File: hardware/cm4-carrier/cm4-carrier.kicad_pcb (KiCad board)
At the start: 2 copper layers, 121 x 76 mm, 0 parts

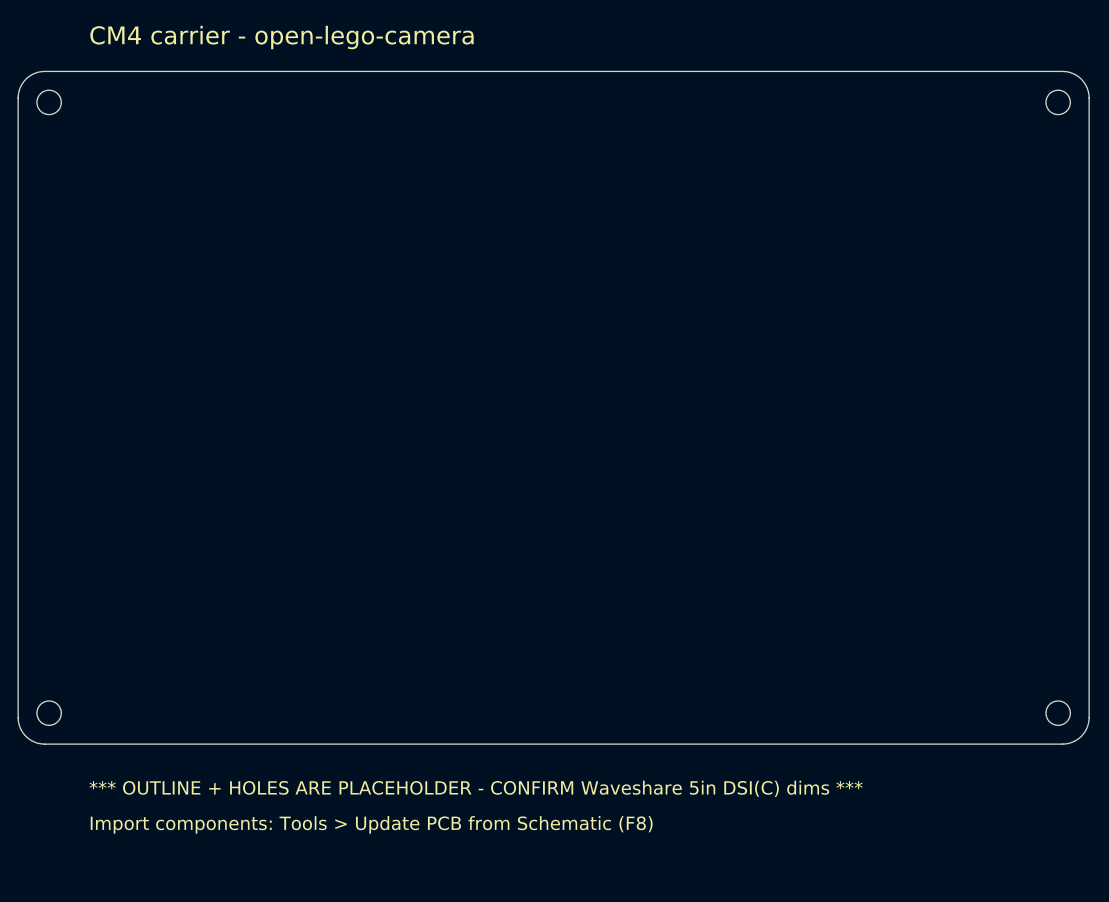
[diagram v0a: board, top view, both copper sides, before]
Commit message: Set PCB outline and mounting holes from Waveshare 5in DSI (C) STEP
Replace the placeholder board dimensions with values extracted from the
supplied Waveshare 5inch DSI LCD (C) STEP model:

- Outline 120.70 x 77.20 mm (display module X/Y extent, 3 mm rounded corners).
- Four M2.5 mounting holes (Ø2.75 mm) on a 113.0 x 68.0 mm rectangle, matching
  the display's STUDS-M2_5XH4 back studs at (+/-56.5, -35.9/+32.1) so the
  carrier bolts directly onto the display.

Silkscreen notes and README updated to the confirmed dimensions.

Co-Authored-By: Claude Opus 4.8 <noreply@anthropic.com>
Claude-Session: https://claude.ai/code/session_015B7X7FE461jFSRaiTFdnFt
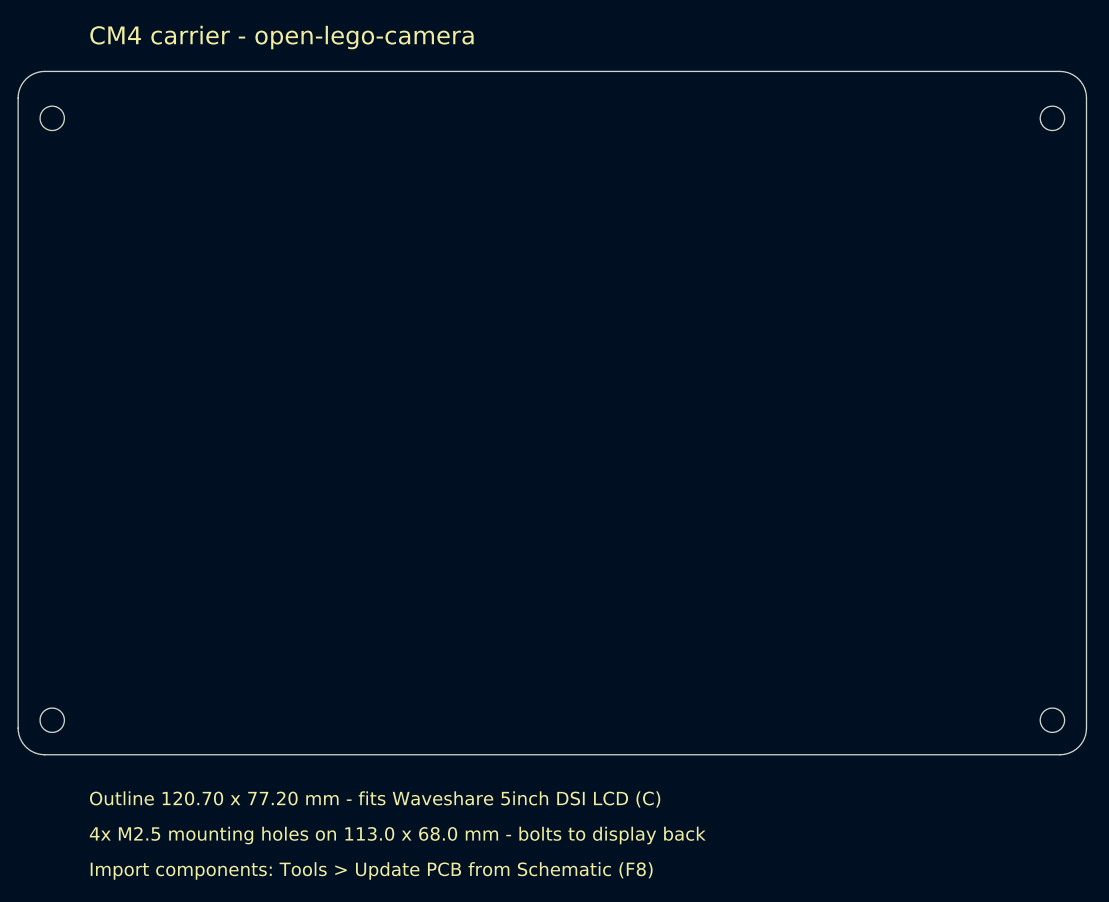
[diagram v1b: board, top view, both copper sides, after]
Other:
- board size 121 x 76 mm -> 120.7 x 77.2 mm
- board text added: "4x M2.5 mounting holes on 113.0 x 68.0 mm - bolts to display back"
- board text added: "Outline 120.70 x 77.20 mm - fits Waveshare 5inch DSI LCD (C)"
- board text removed: "*** OUTLINE + HOLES ARE PLACEHOLDER - CONFIRM Waveshare 5in DSI(C) dims ***"
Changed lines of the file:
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@@
 	)
 	(net 0 "")
-	(gr_line (start 63.000 40.000) (end 178.000 40.000)
+	(gr_line (start 63.000 40.000) (end 177.700 40.000)
 		(stroke (width 0.1) (type solid)) (layer "Edge.Cuts"))
-	(gr_line (start 181.000 43.000) (end 181.000 113.000)
+	(gr_line (start 180.700 43.000) (end 180.700 114.200)
 		(stroke (width 0.1) (type solid)) (layer "Edge.Cuts"))
-	(gr_line (start 178.000 116.000) (end 63.000 116.000)
+	(gr_line (start 177.700 117.200) (end 63.000 117.200)
 		(stroke (width 0.1) (type solid)) (layer "Edge.Cuts"))
-	(gr_line (start 60.000 113.000) (end 60.000 43.000)
+	(gr_line (start 60.000 114.200) (end 60.000 43.000)
 		(stroke (width 0.1) (type solid)) (layer "Edge.Cuts"))
 	(gr_arc (start 60.000 43.000) (mid 60.879 40.879) (end 63.000 40.000)
 		(stroke (width 0.1) (type solid)) (layer "Edge.Cuts"))
-	(gr_arc (start 178.000 40.000) (mid 180.121 40.879) (end 181.000 43.000)
+	(gr_arc (start 177.700 40.000) (mid 179.821 40.879) (end 180.700 43.000)
 		(stroke (width 0.1) (type solid)) (layer "Edge.Cuts"))
-	(gr_arc (start 181.000 113.000) (mid 180.121 115.121) (end 178.000 116.000)
+	(gr_arc (start 180.700 114.200) (mid 179.821 116.321) (end 177.700 117.200)
 		(stroke (width 0.1) (type solid)) (layer "Edge.Cuts"))
-	(gr_arc (start 63.000 116.000) (mid 60.879 115.121) (end 60.000 113.000)
+	(gr_arc (start 63.000 117.200) (mid 60.879 116.321) (end 60.000 114.200)
 		(stroke (width 0.1) (type solid)) (layer "Edge.Cuts"))
-	(gr_circle (center 63.500 43.500) (end 64.875 43.500)
+	(gr_circle (center 63.850 45.300) (end 65.225 45.300)
 		(stroke (width 0.1) (type solid)) (fill none) (layer "Edge.Cuts"))
-	(gr_circle (center 177.500 43.500) (end 178.875 43.500)
+	(gr_circle (center 176.850 45.300) (end 178.225 45.300)
 		(stroke (width 0.1) (type solid)) (fill none) (layer "Edge.Cuts"))
-	(gr_circle (center 63.500 112.500) (end 64.875 112.500)
+	(gr_circle (center 63.850 113.300) (end 65.225 113.300)
 		(stroke (width 0.1) (type solid)) (fill none) (layer "Edge.Cuts"))
-	(gr_circle (center 177.500 112.500) (end 178.875 112.500)
+	(gr_circle (center 176.850 113.300) (end 178.225 113.300)
 		(stroke (width 0.1) (type solid)) (fill none) (layer "Edge.Cuts"))
 	(gr_text "CM4 carrier - open-lego-camera" (at 68.000 36.000)
 		(layer "F.SilkS")
 		(effects (font (size 2.0 2.0) (thickness 0.30)) (justify left)))
-	(gr_text "*** OUTLINE + HOLES ARE PLACEHOLDER - CONFIRM Waveshare 5in DSI(C) dims ***" (at 68.000 121.000)
+	(gr_text "Outline 120.70 x 77.20 mm - fits Waveshare 5inch DSI LCD (C)" (at 68.000 122.200)
 		(layer "F.SilkS")
 		(effects (font (size 1.5 1.5) (thickness 0.22)) (justify left)))
-	(gr_text "Import components: Tools > Update PCB from Schematic (F8)" (at 68.000 125.000)
+	(gr_text "4x M2.5 mounting holes on 113.0 x 68.0 mm - bolts to display back" (at 68.000 126.200)
 		(layer "F.SilkS")
 		(effects (font (size 1.5 1.5) (thickness 0.22)) (justify left)))
+	(gr_text "Import components: Tools > Update PCB from Schematic (F8)" (at 68.000 130.200)
+		(layer "F.SilkS")
+		(effects (font (size 1.5 1.5) (thickness 0.22)) (justify left)))

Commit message: PCB: MountingHole footprints + FPC connector keepout
- Replace the four Edge.Cuts hole cutouts with proper KiCad MountingHole
  footprints (H1-H4, MountingHole_2.7mm_M2.5, unplated np_thru_hole pads) at
  the display's M2.5 stud positions, so they are BOM/DRC-aware.
- Add a keepout rule area ("Display FPC connector clearance") over the display's
  back-side DSI FFC connector so no copper/components sit where it protrudes
  into the standoff gap, with a dashed Cmts.User outline and silkscreen note.

The exact FFC connector could not be labelled from the STEP assembly graph, so
the keepout is a single parameterised rectangle placed at the best-estimate
position (board-local ~(10,42) mm); README lists the other candidate connector
centres from the STEP so it can be moved. Kept as a keepout (not a board
cutout) since the studs give ~8 mm clearance.

Co-Authored-By: Claude Opus 4.8 <noreply@anthropic.com>
Claude-Session: https://claude.ai/code/session_015B7X7FE461jFSRaiTFdnFt
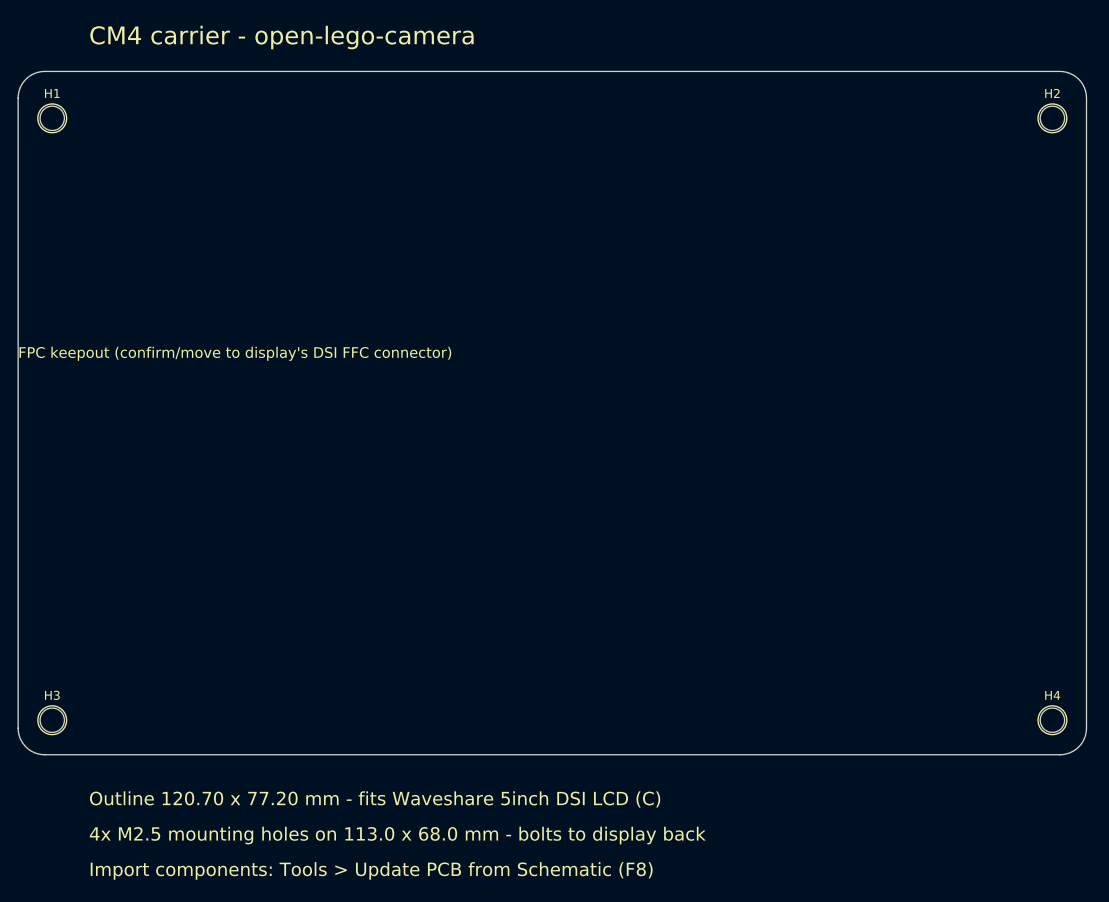
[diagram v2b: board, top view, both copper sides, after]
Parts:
- added H1: MountingHole_M2.5, MountingHole:MountingHole_2.7mm_M2.5, F.Cu at (63.9, 45.3)
- added H2: MountingHole_M2.5, MountingHole:MountingHole_2.7mm_M2.5, F.Cu at (176.8, 45.3)
- added H3: MountingHole_M2.5, MountingHole:MountingHole_2.7mm_M2.5, F.Cu at (63.9, 113.3)
- added H4: MountingHole_M2.5, MountingHole:MountingHole_2.7mm_M2.5, F.Cu at (176.8, 113.3)
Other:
- outline, holes or cut-outs redrawn
- board text added: "FPC keepout (confirm/move to display's DSI FFC connector)"
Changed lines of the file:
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@@
 	(gr_arc (start 63.000 117.200) (mid 60.879 116.321) (end 60.000 114.200)
 		(stroke (width 0.1) (type solid)) (layer "Edge.Cuts"))
-	(gr_circle (center 63.850 45.300) (end 65.225 45.300)
-		(stroke (width 0.1) (type solid)) (fill none) (layer "Edge.Cuts"))
-	(gr_circle (center 176.850 45.300) (end 178.225 45.300)
-		(stroke (width 0.1) (type solid)) (fill none) (layer "Edge.Cuts"))
-	(gr_circle (center 63.850 113.300) (end 65.225 113.300)
-		(stroke (width 0.1) (type solid)) (fill none) (layer "Edge.Cuts"))
-	(gr_circle (center 176.850 113.300) (end 178.225 113.300)
-		(stroke (width 0.1) (type solid)) (fill none) (layer "Edge.Cuts"))
+	(footprint "MountingHole:MountingHole_2.7mm_M2.5"
+		(layer "F.Cu")
+		(at 63.850 45.300)
+		(descr "Mounting hole 2.75mm, no annular ring, M2.5")
+		(attr exclude_from_pos_files exclude_from_bom allow_missing_courtyard)
+		(property "Reference" "H1" (at 0 -2.77 0) (layer "F.SilkS")
+			(effects (font (size 1 1) (thickness 0.15))))
+		(property "Value" "MountingHole_M2.5" (at 0 2.77 0) (layer "F.Fab") (hide yes)
+			(effects (font (size 1 1) (thickness 0.15))))
+		(fp_circle (center 0 0) (end 1.625 0) (stroke (width 0.15) (type solid)) (fill none) (layer "F.SilkS"))
+		(fp_circle (center 0 0) (end 1.875 0) (stroke (width 0.05) (type solid)) (fill none) (layer "F.CrtYd"))
+		(pad "" np_thru_hole circle (at 0 0) (size 2.750 2.750) (drill 2.750) (layers "*.Cu" "*.Mask"))
+	)
+	(footprint "MountingHole:MountingHole_2.7mm_M2.5"
+		(layer "F.Cu")
+		(at 176.850 45.300)
+		(descr "Mounting hole 2.75mm, no annular ring, M2.5")
+		(attr exclude_from_pos_files exclude_from_bom allow_missing_courtyard)
+		(property "Reference" "H2" (at 0 -2.77 0) (layer "F.SilkS")
+			(effects (font (size 1 1) (thickness 0.15))))
+		(property "Value" "MountingHole_M2.5" (at 0 2.77 0) (layer "F.Fab") (hide yes)
+			(effects (font (size 1 1) (thickness 0.15))))
+		(fp_circle (center 0 0) (end 1.625 0) (stroke (width 0.15) (type solid)) (fill none) (layer "F.SilkS"))
+		(fp_circle (center 0 0) (end 1.875 0) (stroke (width 0.05) (type solid)) (fill none) (layer "F.CrtYd"))
+		(pad "" np_thru_hole circle (at 0 0) (size 2.750 2.750) (drill 2.750) (layers "*.Cu" "*.Mask"))
+	)
+	(footprint "MountingHole:MountingHole_2.7mm_M2.5"
+		(layer "F.Cu")
+		(at 63.850 113.300)
+		(descr "Mounting hole 2.75mm, no annular ring, M2.5")
+		(attr exclude_from_pos_files exclude_from_bom allow_missing_courtyard)
+		(property "Reference" "H3" (at 0 -2.77 0) (layer "F.SilkS")
+			(effects (font (size 1 1) (thickness 0.15))))
+		(property "Value" "MountingHole_M2.5" (at 0 2.77 0) (layer "F.Fab") (hide yes)
+			(effects (font (size 1 1) (thickness 0.15))))
+		(fp_circle (center 0 0) (end 1.625 0) (stroke (width 0.15) (type solid)) (fill none) (layer "F.SilkS"))
+		(fp_circle (center 0 0) (end 1.875 0) (stroke (width 0.05) (type solid)) (fill none) (layer "F.CrtYd"))
+		(pad "" np_thru_hole circle (at 0 0) (size 2.750 2.750) (drill 2.750) (layers "*.Cu" "*.Mask"))
+	)
+	(footprint "MountingHole:MountingHole_2.7mm_M2.5"
+		(layer "F.Cu")
+		(at 176.850 113.300)
+		(descr "Mounting hole 2.75mm, no annular ring, M2.5")
+		(attr exclude_from_pos_files exclude_from_bom allow_missing_courtyard)
+		(property "Reference" "H4" (at 0 -2.77 0) (layer "F.SilkS")
+			(effects (font (size 1 1) (thickness 0.15))))
+		(property "Value" "MountingHole_M2.5" (at 0 2.77 0) (layer "F.Fab") (hide yes)
+			(effects (font (size 1 1) (thickness 0.15))))
+		(fp_circle (center 0 0) (end 1.625 0) (stroke (width 0.15) (type solid)) (fill none) (layer "F.SilkS"))
+		(fp_circle (center 0 0) (end 1.875 0) (stroke (width 0.05) (type solid)) (fill none) (layer "F.CrtYd"))
+		(pad "" np_thru_hole circle (at 0 0) (size 2.750 2.750) (drill 2.750) (layers "*.Cu" "*.Mask"))
+	)
+	(zone (net 0) (net_name "") (layers "F.Cu" "B.Cu")
+		(name "Display FPC connector clearance") (hatch edge 0.5)
+		(connect_pads (clearance 0)) (min_thickness 0.25) (filled_areas_thickness no)
+		(keepout (tracks not_allowed) (vias not_allowed) (pads not_allowed) (copperpour not_allowed) (footprints not_allowed))
+		(fill (thermal_gap 0.5) (thermal_bridge_width 0.5))
+		(polygon (pts (xy 60.000 73.300) (xy 80.000 73.300) (xy 80.000 91.300) (xy 60.000 91.300)))
+	)
+	(gr_line (start 60.000 73.300) (end 80.000 73.300) (stroke (width 0.12) (type dash)) (layer "Cmts.User"))
+	(gr_line (start 80.000 73.300) (end 80.000 91.300) (stroke (width 0.12) (type dash)) (layer "Cmts.User"))
+	(gr_line (start 80.000 91.300) (end 60.000 91.300) (stroke (width 0.12) (type dash)) (layer "Cmts.User"))
+	(gr_line (start 60.000 91.300) (end 60.000 73.300) (stroke (width 0.12) (type dash)) (layer "Cmts.User"))
+	(gr_text "FPC keepout (confirm/move to display's DSI FFC connector)" (at 60.000 71.800)
+		(layer "F.SilkS")
+		(effects (font (size 1.2 1.2) (thickness 0.18)) (justify left)))
 	(gr_text "CM4 carrier - open-lego-camera" (at 68.000 36.000)
 		(layer "F.SilkS")

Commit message: PCB: switch to 4-layer stackup
Define the board as 4-layer (F.Cu / In1.Cu / In2.Cu / B.Cu) with a physical
1.6 mm FR4 stackup (0.035 mm outer / 0.0152 mm inner copper, ENIG) suited to
the CM4's high-speed CSI/DSI/PCIe/USB nets. Extend the FPC-connector keepout
across all four copper layers. README updated.

Co-Authored-By: Claude Opus 4.8 <noreply@anthropic.com>
Claude-Session: https://claude.ai/code/session_015B7X7FE461jFSRaiTFdnFt
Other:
- copper layers 2 -> 4
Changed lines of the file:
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@@
 	(layers
 		(0 "F.Cu" signal)
+		(1 "In1.Cu" signal)
+		(2 "In2.Cu" signal)
 		(31 "B.Cu" signal)
 		(32 "B.Adhes" user "B.Adhesive")
@@
 	)
 	(setup
+		(stackup
+			(layer "F.SilkS" (type "Top Silk Screen"))
+			(layer "F.Paste" (type "Top Solder Paste"))
+			(layer "F.Mask" (type "Top Solder Mask") (color "Green") (thickness 0.01))
+			(layer "F.Cu" (type "copper") (thickness 0.035))
+			(layer "dielectric 1" (type "prepreg") (thickness 0.2104) (material "FR4") (epsilon_r 4.5) (loss_tangent 0.02))
+			(layer "In1.Cu" (type "copper") (thickness 0.0152))
+			(layer "dielectric 2" (type "core") (thickness 1.065) (material "FR4") (epsilon_r 4.5) (loss_tangent 0.02))
+			(layer "In2.Cu" (type "copper") (thickness 0.0152))
+			(layer "dielectric 3" (type "prepreg") (thickness 0.2104) (material "FR4") (epsilon_r 4.5) (loss_tangent 0.02))
+			(layer "B.Cu" (type "copper") (thickness 0.035))
+			(layer "B.Mask" (type "Bottom Solder Mask") (color "Green") (thickness 0.01))
+			(layer "B.Paste" (type "Bottom Solder Paste"))
+			(layer "B.SilkS" (type "Bottom Silk Screen"))
+			(copper_finish "ENIG")
+			(dielectric_constraints no)
+		)
 		(pad_to_mask_clearance 0)
 		(allow_soldermask_bridges_in_footprints no)
@@
 		(pad "" np_thru_hole circle (at 0 0) (size 2.750 2.750) (drill 2.750) (layers "*.Cu" "*.Mask"))
 	)
-	(zone (net 0) (net_name "") (layers "F.Cu" "B.Cu")
+	(zone (net 0) (net_name "") (layers "F.Cu" "In1.Cu" "In2.Cu" "B.Cu")
 		(name "Display FPC connector clearance") (hatch edge 0.5)
 		(connect_pads (clearance 0)) (min_thickness 0.25) (filled_areas_thickness no)
